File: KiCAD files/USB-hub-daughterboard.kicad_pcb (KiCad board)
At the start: 2 copper layers, 86 x 33 mm, 53 parts, among them J1 TYPE-C-31-M12_13, J2 USB_A, J3 USB_A, J4 SM04B-SRSS-TB(LF)(SN), J5 SM04B-SRSS-TB(LF)(SN), U1 USBLC6-2SC6, U2 AP2112K-3.3, U3 USB2514B_Bi, U4 USBLC6-2SC6, U5 USBLC6-2SC6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

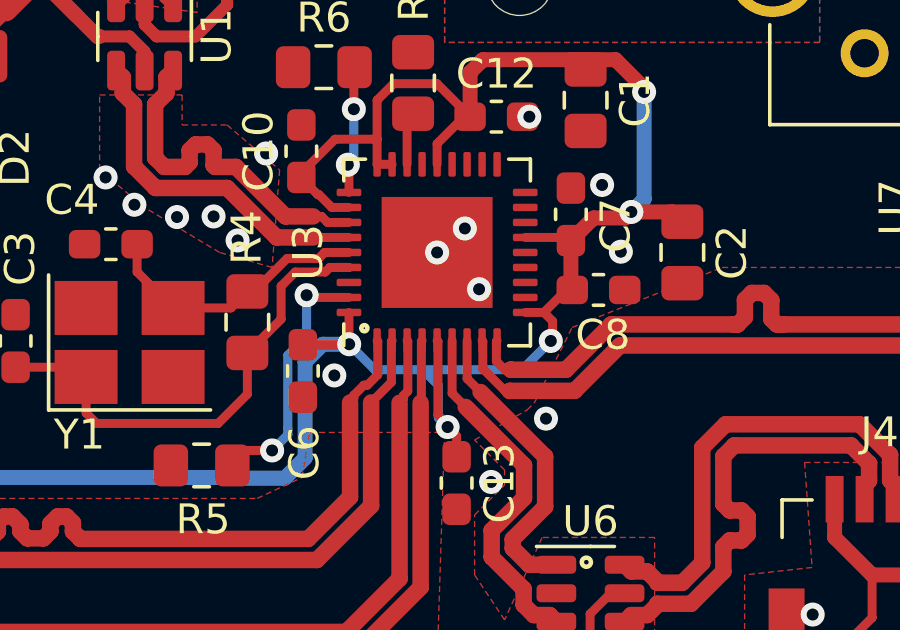
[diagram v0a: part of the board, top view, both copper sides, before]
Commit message: Slightly improved routing, made PCB 1.2mm thick
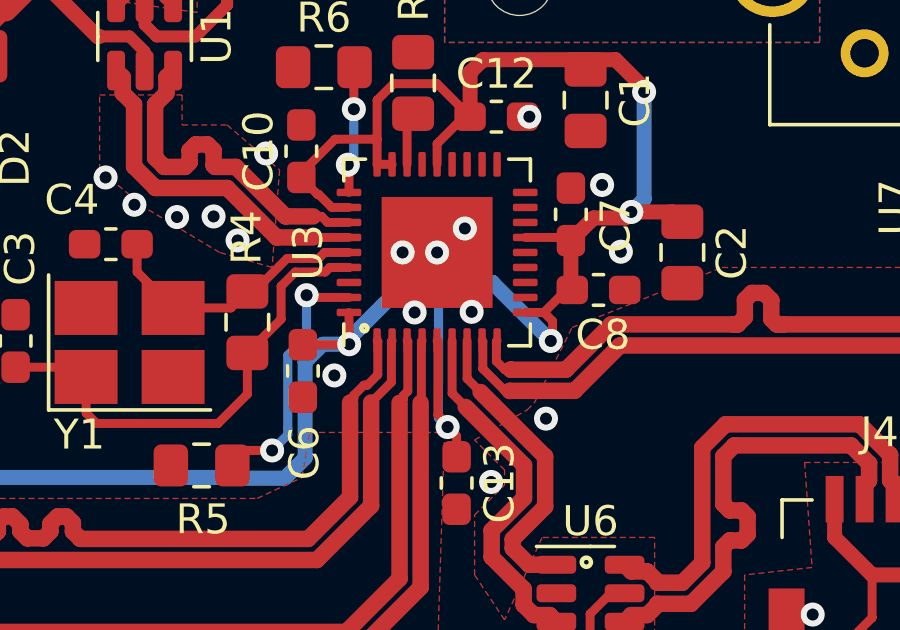
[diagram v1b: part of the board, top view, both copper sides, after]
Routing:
- net GND: track 5.43 -> 10.2 mm, vias 29 -> 31
- net +3V3: track 79.1 -> 82.9 mm
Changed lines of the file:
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@@
   (segment (start 10.25 16) (end 10.25 15.45) (width 0.5) (layer "F.Cu") (net 1))
   (segment (start -19.07258 19.90742) (end -19 19.98) (width 0.5) (layer "F.Cu") (net 1))
+  (segment (start 10.25 17.25) (end 9.5 18) (width 0.3) (layer "F.Cu") (net 1))
+  (segment (start 10.25 16.827759) (end 11.402166 17.979925) (width 0.3) (layer "F.Cu") (net 1))
   (segment (start -18.525 18) (end -19.07258 18.54758) (width 0.5) (layer "F.Cu") (net 1))
   (segment (start -17.8625 18) (end -18.525 18) (width 0.5) (layer "F.Cu") (net 1))
+  (segment (start 10.25 16) (end 10.25 16.827759) (width 0.3) (layer "F.Cu") (net 1))
   (segment (start 10.25 15.45) (end 10.3 15.4) (width 0.5) (layer "F.Cu") (net 1))
+  (segment (start 10.25 16) (end 10.25 17.25) (width 0.3) (layer "F.Cu") (net 1))
   (segment (start -19.07258 18.54758) (end -19.07258 19.90742) (width 0.5) (layer "F.Cu") (net 1))
+  (via (at 11.402166 17.979925) (size 0.8) (drill 0.4) (layers "F.Cu" "B.Cu") (net 1))
   (via (at -22.7 28.12) (size 0.8) (drill 0.4) (layers "F.Cu" "B.Cu") (free) (net 1))
   (via (at -19.45 22.09) (size 0.8) (drill 0.4) (layers "F.Cu" "B.Cu") (free) (net 1))
   (via (at 3.6 15.6) (size 0.8) (drill 0.4) (layers "F.Cu" "B.Cu") (free) (net 1))
   (via (at 10.25 16) (size 0.8) (drill 0.4) (layers "F.Cu" "B.Cu") (net 1))
+  (via (at 9.5 18) (size 0.8) (drill 0.4) (layers "F.Cu" "B.Cu") (net 1))
   (via (at 22.77 28.07) (size 0.8) (drill 0.4) (layers "F.Cu" "B.Cu") (free) (net 1))
   (via (at -0.75 5.75) (size 0.8) (drill 0.4) (layers "F.Cu" "B.Cu") (free) (net 1))
@@
   (via (at -25.43 21.11) (size 0.8) (drill 0.4) (layers "F.Cu" "B.Cu") (free) (net 1))
   (via (at 16.375 15.975) (size 0.8) (drill 0.4) (layers "F.Cu" "B.Cu") (free) (net 1))
-  (via (at 11.65 17.225) (size 0.8) (drill 0.4) (layers "F.Cu" "B.Cu") (net 1))
+  (via (at 9.1 16) (size 0.8) (drill 0.4) (layers "F.Cu" "B.Cu") (net 1))
   (via (at 13.325 11.475) (size 0.8) (drill 0.4) (layers "F.Cu" "B.Cu") (free) (net 1))
   (via (at -22.75 10) (size 0.8) (drill 0.4) (layers "F.Cu" "B.Cu") (free) (net 1))
@@
   (via (at -6 21.55) (size 0.8) (drill 0.4) (layers "F.Cu" "B.Cu") (net 2))
   (via (at -6.025 22.575) (size 0.8) (drill 0.4) (layers "F.Cu" "B.Cu") (net 2))
-  (segment (start 8.17 19.91) (end 9.78 19.91) (width 0.3) (layer "B.Cu") (net 2))
+  (segment (start 10.3 17) (end 12.1 17) (width 0.5) (layer "B.Cu") (net 2))
+  (segment (start 10.3 20.41) (end 10.29 20.42) (width 0.3) (layer "B.Cu") (net 2))
+  (segment (start 7.32 18.88) (end 9.2 17) (width 0.5) (layer "B.Cu") (net 2))
+  (segment (start 7.32 19.06) (end 7.32 18.88) (width 0.5) (layer "B.Cu") (net 2))
+  (segment (start 10.29 21.51) (end 10.6 21.82) (width 0.3) (layer "B.Cu") (net 2))
   (segment (start 5.85 22.85) (end 5.175 23.525) (width 0.5) (layer "B.Cu") (net 2))
   (segment (start 7.32 19.06) (end 6.44 19.06) (width 0.5) (layer "B.Cu") (net 2))
-  (segment (start 7.32 19.06) (end 8.17 19.91) (width 0.3) (layer "B.Cu") (net 2))
-  (segment (start 10.29 21.51) (end 10.6 21.82) (width 0.3) (layer "B.Cu") (net 2))
+  (segment (start 10.3 20.41) (end 10.3 17) (width 0.3) (layer "B.Cu") (net 2))
+  (segment (start 7.32 19.06) (end 7.34 19.06) (width 0.3) (layer "B.Cu") (net 2))
   (segment (start 5.85 19.65) (end 5.85 22.85) (width 0.5) (layer "B.Cu") (net 2))
-  (segment (start 10.29 20.42) (end 10.29 21.51) (width 0.3) (layer "B.Cu") (net 2))
-  (segment (start 13.08 19.91) (end 14.04 18.95) (width 0.3) (layer "B.Cu") (net 2))
-  (segment (start 9.78 19.91) (end 13.08 19.91) (width 0.3) (layer "B.Cu") (net 2))
-  (segment (start 9.78 19.91) (end 10.29 20.42) (width 0.3) (layer "B.Cu") (net 2))
+  (segment (start 12.1 17) (end 12.1 17.01) (width 0.5) (layer "B.Cu") (net 2))
   (segment (start 17.15 10.65) (end 17.15 14.225) (width 0.5) (layer "B.Cu") (net 2))
   (segment (start -5.025 23.5) (end -5.975 22.55) (width 0.5) (layer "B.Cu") (net 2))
@@
   (segment (start 3.775 23.525) (end 3.75 23.5) (width 0.5) (layer "B.Cu") (net 2))
   (segment (start 5.175 23.525) (end 3.775 23.525) (width 0.5) (layer "B.Cu") (net 2))
+  (segment (start 12.1 17.01) (end 14.04 18.95) (width 0.5) (layer "B.Cu") (net 2))
   (segment (start 3.75 23.5) (end -5.025 23.5) (width 0.5) (layer "B.Cu") (net 2))
+  (segment (start 10.29 20.42) (end 10.29 21.51) (width 0.3) (layer "B.Cu") (net 2))
   (segment (start 6.44 19.06) (end 5.85 19.65) (width 0.5) (layer "B.Cu") (net 2))
+  (segment (start 9.2 17) (end 10.3 17) (width 0.5) (layer "B.Cu") (net 2))
   (segment (start -8.28 14.27) (end -7.92 13.91) (width 0.5) (layer "F.Cu") (net 3))
   (segment (start 16.5 27.36) (end 16.04 27.36) (width 0.3) (layer "F.Cu") (net 3))
